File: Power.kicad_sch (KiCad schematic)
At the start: 46 parts, among them U14 TPS54202DDCR, U5 TPS54202DDCR, U8 TPS54202DDCR

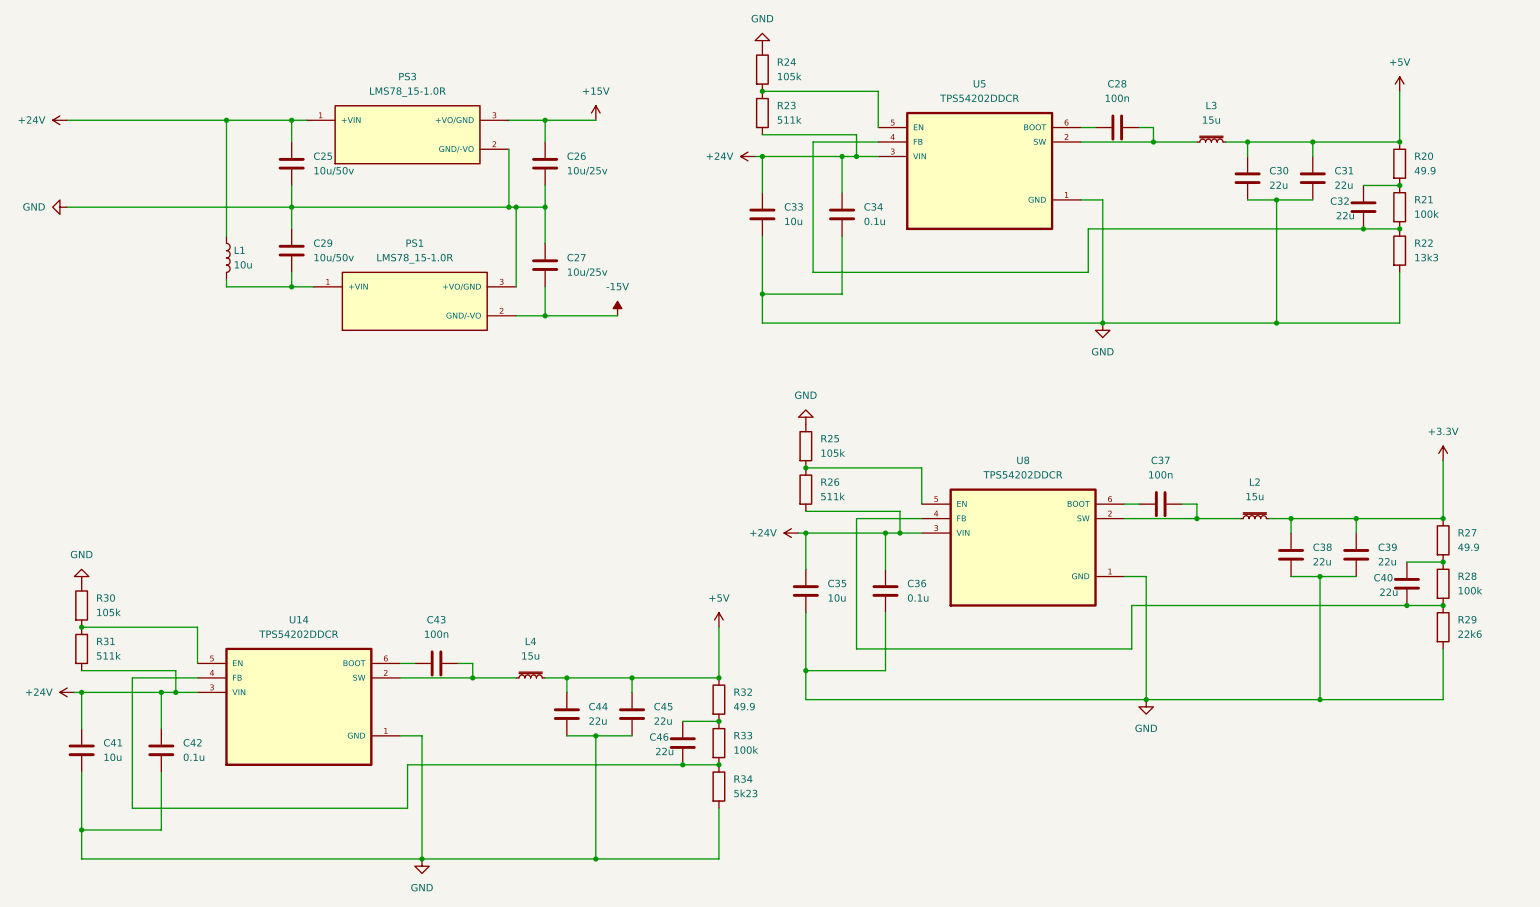
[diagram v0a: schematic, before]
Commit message: Added Footprint
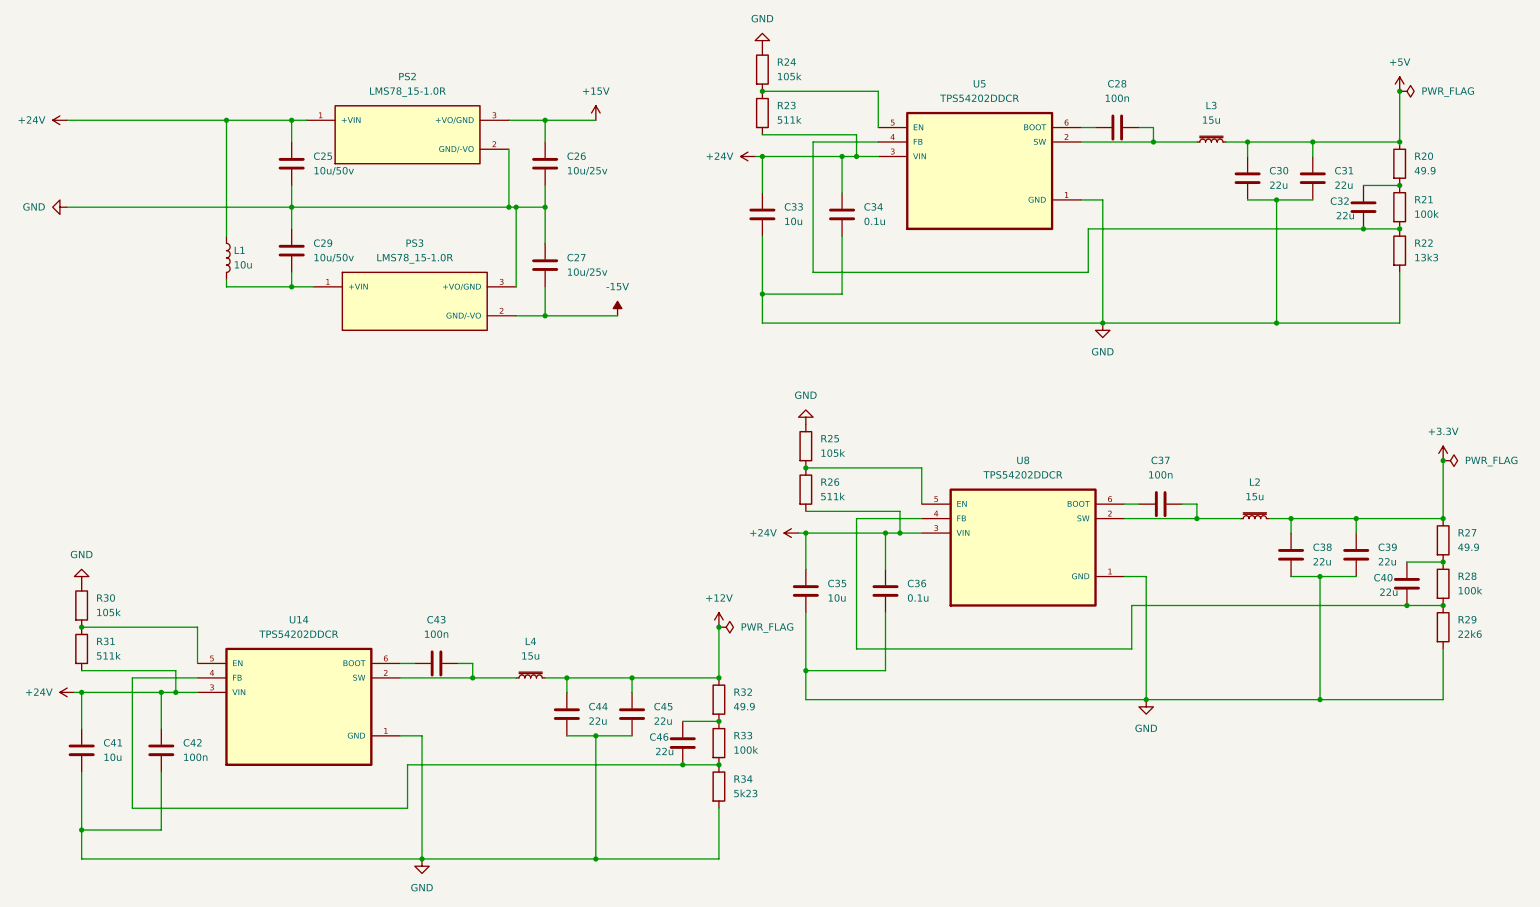
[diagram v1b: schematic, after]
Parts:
- removed PS1: LMS78_15-1.0R, LMS78_15-1.0R:CONV_LMS78_15-1.0R, symbol LMS78_15-1.0R:LMS78_15-1.0R
- added PS2: LMS78_15-1.0R, LMS78_15-1.0R:CONV_LMS78_15-1.0R, symbol LMS78_15-1.0R:LMS78_15-1.0R
- C28, C34, C36, C37, C43: footprint (none) -> Capacitor_SMD:C_0805_2012Metric_Pad1.18x1.45mm_HandSolder
- C30, C31, C32, C38, C39, C40, C44, C45, C46: footprint (none) -> Capacitor_SMD:C_1210_3225Metric_Pad1.33x2.70mm_HandSolder
- C33, C35, C41: footprint (none) -> Capacitor_SMD:C_1206_3216Metric_Pad1.33x1.80mm_HandSolder
- C42: value 0.1u -> 100n; footprint (none) -> Capacitor_SMD:C_0805_2012Metric_Pad1.18x1.45mm_HandSolder
- L1, L2, L3, L4: footprint (none) -> Inductor_SMD:L_1210_3225Metric_Pad1.42x2.65mm_HandSolder
- R20, R21, R22, R23, R24, R25, R26, R27, R28, R29, R30, R31, R32, R33, R34: footprint (none) -> Resistor_SMD:R_0805_2012Metric_Pad1.20x1.40mm_HandSolder
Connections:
- net +15V: now also PS2.3 (+VO/GND); no longer PS3.3 (+VO/GND)
- net +24V: now also PS2.1 (+VIN); no longer PS3.1 (+VIN)
- net +5V: no longer C44.1, C45.1, L4.2, R32.1
- net -15V: now also PS3.2 (GND/-VO)
- net GND: now also PS3.3 (+VO/GND), PS2.2 (GND/-VO); no longer PS3.2 (GND/-VO)
- net at C29.2, L1.2: now also PS3.1 (+VIN)
- new net +12V: C44.1, C45.1, L4.2, R32.1

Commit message: Solved errors
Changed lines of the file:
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@@
 				)
 				(justify bottom)
-				(hide yes)
 			)
 		)

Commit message: New PCB Changes
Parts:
- removed PS3: LMS78_15-1.0R, LMS78_15-1.0R:CONV_LMS78_15-1.0R, symbol LMS78_15-1.0R:LMS78_15-1.0R
- removed U14: TPS54202DDCR, TPS54202DDCR:SOT95P280X110-6N, symbol TPS54202DDCR:TPS54202DDCR
- added PS1: LMS78_15-1.0R, Library:CONV_LMS78_15-1.0R, symbol LMS78_15-1.0R:LMS78_15-1.0R
- added U19: TPS54202DDCR, Library:SOT95P280X110-6N, symbol TPS54202DDCR:TPS54202DDCR
- PS2: footprint LMS78_15-1.0R:CONV_LMS78_15-1.0R -> Library:CONV_LMS78_15-1.0R
- U5, U8: footprint TPS54202DDCR:SOT95P280X110-6N -> Library:SOT95P280X110-6N
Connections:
- net +15V: now also PS1.3 (+VO/GND); no longer PS2.3 (+VO/GND)
- net +24V: now also PS1.1 (+VIN), U19.3 (VIN); no longer PS2.1 (+VIN)
- net -15V: now also PS2.2 (GND/-VO)
- net GND: now also PS2.3 (+VO/GND), PS1.2 (GND/-VO), U19.1 (GND); no longer PS2.2 (GND/-VO)
- net at C46.2, R33.2, R34.1: now also U8.4 (FB)
- net at C29.2, L1.2: now also PS2.1 (+VIN)
- net at C32.2, R21.2, R22.1: now also U19.4 (FB); no longer U5.4 (FB)
- net at R25.2, R26.1: now also U5.5 (EN); no longer U8.5 (EN)
- net at R30.2, R31.1: now also U8.5 (EN)
- net at C28.1: now also U19.6 (BOOT); no longer U5.6 (BOOT)
- net at C28.2, L3.1: now also U19.2 (SW); no longer U5.2 (SW)
- net at C43.2, L4.1: now also U8.2 (SW)
- net at C43.1: now also U8.6 (BOOT)
- net at C37.2, L2.1: now also U5.2 (SW); no longer U8.2 (SW)
- net at C40.2, R28.2, R29.1: now also U5.4 (FB); no longer U8.4 (FB)
- net at C37.1: now also U5.6 (BOOT); no longer U8.6 (BOOT)
- net at R23.1, R24.2: now also U19.5 (EN); no longer U5.5 (EN)

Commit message: FInal Changes in Schgematic
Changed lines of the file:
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@@
 	(wire
 		(pts
-			(xy 118.11 36.83) (xy 120.65 36.83)
+			(xy 118.11 36.83) (xy 128.27 36.83)
 		)
 		(stroke
@@
 	(wire
 		(pts
-			(xy 120.65 71.12) (xy 124.46 71.12)
+			(xy 120.65 71.12) (xy 130.81 71.12)
 		)
 		(stroke
@@
 	(symbol
 		(lib_id "power:+15V")
-		(at 120.65 36.83 0)
+		(at 128.27 36.83 0)
 		(unit 1)
 		(exclude_from_sim no)
@@
 		(fields_autoplaced yes)
 		(property "Reference" "#PWR045"
-			(at 120.65 40.64 0)
+			(at 128.27 40.64 0)
 			(effects
 				(font
@@
 		)
 		(property "Value" "+15V"
-			(at 120.65 31.75 0)
+			(at 128.27 31.75 0)
 			(effects
 				(font
@@
 		)
 		(property "Footprint" ""
-			(at 120.65 36.83 0)
+			(at 128.27 36.83 0)
 			(effects
 				(font
@@
 		)
 		(property "Datasheet" ""
-			(at 120.65 36.83 0)
+			(at 128.27 36.83 0)
 			(effects
 				(font
@@
 		)
 		(property "Description" "Power symbol creates a global label with name \"+15V\""
-			(at 120.65 36.83 0)
+			(at 128.27 36.83 0)
 			(effects
 				(font
@@
 		(on_board yes)
 		(dnp no)
-		(fields_autoplaced yes)
 		(property "Reference" "#FLG08"
 			(at 120.65 73.025 0)
@@
 	(symbol
 		(lib_id "power:-15V")
-		(at 124.46 71.12 0)
+		(at 130.81 71.12 0)
 		(unit 1)
 		(exclude_from_sim no)
@@
 		(fields_autoplaced yes)
 		(property "Reference" "#PWR046"
-			(at 124.46 74.93 0)
+			(at 130.81 74.93 0)
 			(effects
 				(font
@@
 		)
 		(property "Value" "-15V"
-			(at 124.46 66.04 0)
+			(at 130.81 66.04 0)
 			(effects
 				(font
@@
 		)
 		(property "Footprint" ""
-			(at 124.46 71.12 0)
+			(at 130.81 71.12 0)
 			(effects
 				(font
@@
 		)
 		(property "Datasheet" ""
-			(at 124.46 71.12 0)
+			(at 130.81 71.12 0)
 			(effects
 				(font
@@
 		)
 		(property "Description" "Power symbol creates a global label with name \"-15V\""
-			(at 124.46 71.12 0)
+			(at 130.81 71.12 0)
 			(effects
 				(font

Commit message: Deleted Uneeded Portion
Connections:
- net +24V renamed +24
